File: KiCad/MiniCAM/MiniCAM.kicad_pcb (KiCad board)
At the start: 4 copper layers, 25.4 x 25.4 mm, 66 parts, among them J1 SMA-J-P-H-RA-TH1, J2 Conn_01x02, J3 Conn_01x03, J4 Conn_02x03_Odd_Even, U1 NCV8154MW180280TBG, U2 DS90UB933-Q1, U3 MT9P031, U4 SiT_2.5mmx2mm

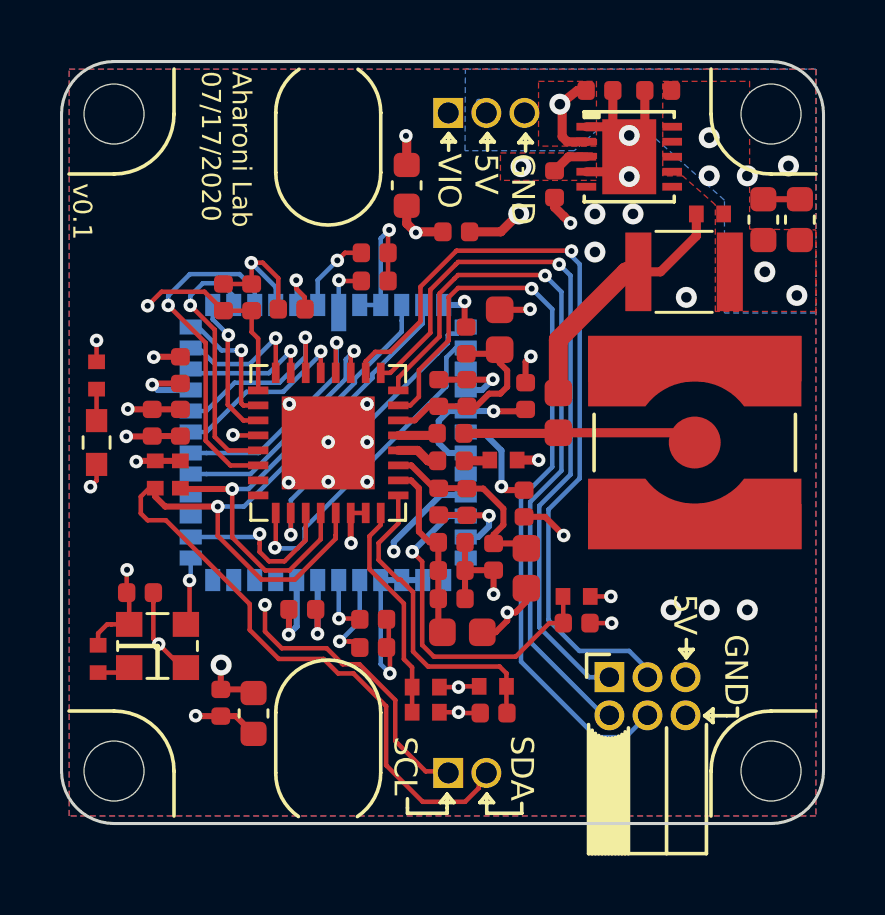
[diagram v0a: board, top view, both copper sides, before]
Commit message: Add connection to TRIG pin of sensor along with 0 resistors
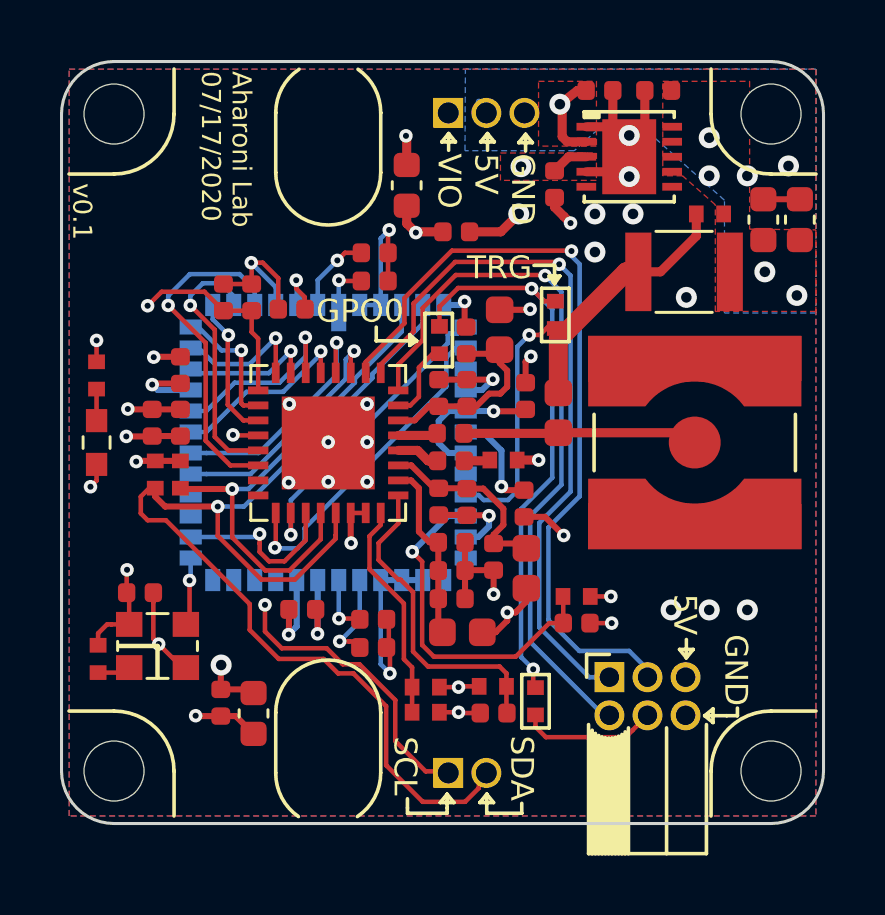
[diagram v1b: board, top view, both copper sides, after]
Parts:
- added R11: 0, .Resistor:R_0402_1005Metric_ERJ_L, F.Cu at (118.1, 33.8)
- added R12: 0, .Resistor:R_0402_1005Metric_ERJ_L, F.Cu at (117.4, 46.7)
- added R13: 0, .Resistor:R_0402_1005Metric_ERJ_L, F.Cu at (114.2, 34.7)
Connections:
- J4 pad 4: /GPO0 -> Net-(J4-Pad4)
- U2 pad 15: /GPO0 -> Net-(R13-Pad1)
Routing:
- net /GPO0: track 26.1 -> 19.2 mm, vias 1 -> 2
- net /TRIGGER: track 3.37 -> 8.19 mm
- net Net-(J4-Pad4): track 0.00 -> 4.58 mm
- net Net-(R13-Pad1): track 0.00 -> 2.66 mm
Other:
- board text added: "GPO0"
- board text added: "TRG"

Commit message: Generate BOM, PnP, Gerbers. Check and correct DRC errors. v0.1
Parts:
- R5, R6: value 1K -> 2K
- moved R11 1.90 mm to (119.4, 32.5)
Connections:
- R8 pad 1: +2V8 -> +1V8
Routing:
- net +1V8: track 74.3 -> 78.7 mm, vias 8 -> 9
- net /TRIGGER: track 8.19 -> 10.2 mm
- net /GPO0: track 19.2 -> 20.9 mm
- net +2V8: track 36.8 -> 36.2 mm
- net GND: track 60.9 -> 61.4 mm
- net +5V: vias 6 -> 5
